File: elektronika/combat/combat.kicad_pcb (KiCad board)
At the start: 2 copper layers, 8 parts, among them J1 Conn_01x04_Pin, U2 TB6612FNG, U3 AMS1117, U3 L78M05CDT, U4 przetwornica

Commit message: płytka pcb bez footprinta
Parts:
- removed U2: TB6612FNG, Package_SO:SSOP-24_5.3x8.2mm_P0.65mm
- removed the U3 at (195.0, 100.7)
- removed the U3 at (163.5, 115.4)
- added J2: naped_prawy, TerminalBlock:TerminalBlock_MaiXu_MX126-5.0-02P_1x02_P5.00mm, F.Cu at (196.5, 137.0)
- added J3: naped_lewy, TerminalBlock:TerminalBlock_MaiXu_MX126-5.0-02P_1x02_P5.00mm, F.Cu at (196.5, 147.1)
- added TB1: POLOLU-713, foots:SHIELD_POLOLU-713, F.Cu at (241.7, 109.4)
- added U1: ESP32-S3-WROOM-1, Espressif:ESP32-S3-WROOM-1, F.Cu at (222.4, 115.1)
- added U3: AMS1117, Package_TO_SOT_SMD:SOT-223-3_TabPin2, F.Cu at (197.4, 156.4)
- R1: value 1k -> 240
- R2: value 1k -> 390
- moved U4 66.3 mm to (208.2, 149.2)
- moved R2 53.7 mm to (207.1, 160.2)
- moved R1 53.7 mm to (207.1, 157.7)
- moved D1 45.2 mm to (210.9, 158.5)
- moved J1 40.5 mm to (207.3, 134.3)
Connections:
- J1 pad 1: unconnected-(J1-Pin_1-Pad1) -> RX
- J1 pad 2: unconnected-(J1-Pin_2-Pad2) -> TX
- J1 pad 3: unconnected-(J1-Pin_3-Pad3) -> +5V
- J1 pad 4: unconnected-(J1-Pin_4-Pad4) -> GND

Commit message: gotowy footprint
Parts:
- added C1: 10uF, Capacitor_SMD:C_0805_2012Metric_Pad1.18x1.45mm_HandSolder, F.Cu at (205.5, 137.3)
- added C2: 22uF, Capacitor_SMD:C_1210_3225Metric_Pad1.33x2.70mm_HandSolder, F.Cu at (206.1, 133.6)
- added C5: 1u, Capacitor_SMD:C_0603_1608Metric, F.Cu at (159.5, 104.5)
- added D2: RED, LED_SMD:LED_0603_1608Metric, F.Cu at (201.1, 132.8)
- added D3: GREEN, LED_SMD:LED_0603_1608Metric, F.Cu at (201.1, 135.4)
- added D4: BLUE, LED_SMD:LED_0603_1608Metric, F.Cu at (201.1, 138.0)
- added H1: MountingHole, MountingHole:MountingHole_3.2mm_M3, F.Cu at (102.0, 103.5)
- added H2: MountingHole, MountingHole:MountingHole_3.2mm_M3, F.Cu at (103.0, 91.0)
- added H3: MountingHole, MountingHole:MountingHole_3.2mm_M3, F.Cu at (100.5, 122.0)
- added H4: MountingHole, MountingHole:MountingHole_3.2mm_M3, F.Cu at (101.0, 112.5)
- added J4: USB_C_Receptacle_USB2.0_14P, Connector_USB:USB_C_Receptacle_HRO_TYPE-C-31-M-12, F.Cu at (159.9, 123.9)
- added J5: Screw_Terminal_01x03, PCM_SparkFun-Connector:ScrewTerminal_1x03_P3.5mm_Blue, F.Cu at (136.0, 128.0)
- added J6: programator caveman, Connector_PinHeader_2.54mm:PinHeader_2x04_P2.54mm_Vertical, F.Cu at (215.0, 133.4)
- added J7: zasilanie, PCM_SparkFun-Connector:ScrewTerminal_1x02_P3.5mm_Blue, F.Cu at (212.9, 99.6)
- added R10: 5.1K, Resistor_SMD:R_0603_1608Metric, F.Cu at (152.0, 136.9)
- added R11: 5.1K, Resistor_SMD:R_0603_1608Metric, F.Cu at (152.0, 139.4)
- added R5: 5.1K, Resistor_SMD:R_0603_1608Metric, F.Cu at (152.0, 126.9)
- added R6: 1k, Resistor_SMD:R_0603_1608Metric, F.Cu at (152.0, 129.4)
- added R7: 1k, Resistor_SMD:R_0603_1608Metric, F.Cu at (152.0, 131.9)
- added R8: 5.1K, Resistor_SMD:R_0603_1608Metric, F.Cu at (152.0, 134.4)
- added SW1: SW_DIP_x01, foots:gownoklik, F.Cu at (155.4, 69.4)
- added SW3: SW_DIP_x01, foots:gownoklik, F.Cu at (189.5, 70.5)
- added U2: kontroler_bldc, foots:BLDC, F.Cu at (134.6, 74.5)
- J1: value Conn_01x04_Pin -> odbiornik
- J2, J3: footprint TerminalBlock:TerminalBlock_MaiXu_MX126-5.0-02P_1x02_P5.00mm -> PCM_SparkFun-Connector:ScrewTerminal_1x02_P3.5mm_Blue
- R1: value 240 -> 390
- R2: value 390 -> 240
- U3: value AMS1117 -> stabilizator
- moved U4 67.8 mm to (204.5, 81.5)
- moved R1 65.7 mm to (152.0, 121.9)
- moved R2 65.7 mm to (152.0, 124.4)
- moved U1 61.7 mm to (172.5, 78.8)
- moved TB1 61.7 mm to (180.3, 115.9)
- moved D1 51.5 mm to (161.4, 144.5)
- moved J3 48.6 mm to (201.9, 98.9)
- moved J2 38.3 mm to (192.7, 98.9)
- moved U3 25.8 mm to (182.0, 135.8)
- moved J1 17.0 mm to (191.5, 140.4)
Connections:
- J2 pad 1: unconnected-(J2-Pin_1-Pad1) -> B01
- J2 pad 2: unconnected-(J2-Pin_2-Pad2) -> B02
- J3 pad 1: unconnected-(J3-Pin_1-Pad1) -> A01
- J3 pad 2: unconnected-(J3-Pin_2-Pad2) -> A02
- TB1 pad 10: unconnected-(TB1-PWMB-Pad10) -> GPIO10
- TB1 pad 11: unconnected-(TB1-BIN2-Pad11) -> GPIO9
- TB1 pad 12: unconnected-(TB1-BIN1-Pad12) -> GPIO8
- TB1 pad 13: unconnected-(TB1-~{STBY}-Pad13) -> 3V3
- TB1 pad 14: unconnected-(TB1-AIN1-Pad14) -> GPIO5
- TB1 pad 15: unconnected-(TB1-AIN2-Pad15) -> GPIO6
- TB1 pad 16: unconnected-(TB1-PWMA-Pad16) -> GPIO7
- TB1 pad 2: unconnected-(TB1-VCC-Pad2) -> 3V3
- TB1 pad 3: unconnected-(TB1-AO1-Pad3) -> A01
- TB1 pad 4: unconnected-(TB1-AO2-Pad4) -> A02
- TB1 pad 5: unconnected-(TB1-BO2-Pad5) -> B02
- TB1 pad 6: unconnected-(TB1-BO1-Pad6) -> B01
- TB1 pad 7: unconnected-(TB1-VMOT-Pad7) -> 11.1V
- U1 pad 1: Net-(U1-GND-Pad1) -> GND
- U1 pad 10: unconnected-(U1-GPIO17/U1TXD/ADC2_CH6-Pad10) -> RX
- U1 pad 11: unconnected-(U1-GPIO18/U1RXD/ADC2_CH7/CLK_OUT3-Pad11) -> TX
- U1 pad 12: unconnected-(U1-GPIO8/TOUCH8/ADC1_CH7/SUBSPICS1-Pad12) -> GPIO8
- U1 pad 13: unconnected-(U1-GPIO19/U1RTS/ADC2_CH8/CLK_OUT2/USB_D--Pad13) -> D-
- U1 pad 14: unconnected-(U1-GPIO20/U1CTS/ADC2_CH9/CLK_OUT1/USB_D+-Pad14) -> D+
- U1 pad 17: unconnected-(U1-GPIO9/TOUCH9/ADC1_CH8/FSPIHD/SUBSPIHD-Pad17) -> GPIO9
- U1 pad 18: unconnected-(U1-GPIO10/TOUCH10/ADC1_CH9/FSPICS0/FSPIIO4/SUBSPICS0-Pad18) -> GPIO10
- U1 pad 2: unconnected-(U1-3V3-Pad2) -> +3.3V
- U1 pad 23: unconnected-(U1-GPIO21-Pad23) -> GPIO21
- U1 pad 27: unconnected-(U1-GPIO0/BOOT-Pad27) -> GPIO0
- U1 pad 3: unconnected-(U1-EN-Pad3) -> EN
- U1 pad 4: unconnected-(U1-GPIO4/TOUCH4/ADC1_CH3-Pad4) -> ePWM
- U1 pad 40: Net-(U1-GND-Pad1) -> GND
- U1 pad 41: Net-(U1-GND-Pad1) -> GND
- U1 pad 5: unconnected-(U1-GPIO5/TOUCH5/ADC1_CH4-Pad5) -> GPIO5
- U1 pad 6: unconnected-(U1-GPIO6/TOUCH6/ADC1_CH5-Pad6) -> GPIO6
- U1 pad 7: unconnected-(U1-GPIO7/TOUCH7/ADC1_CH6-Pad7) -> GPIO7
- U4 pad 1: (no net) -> GND

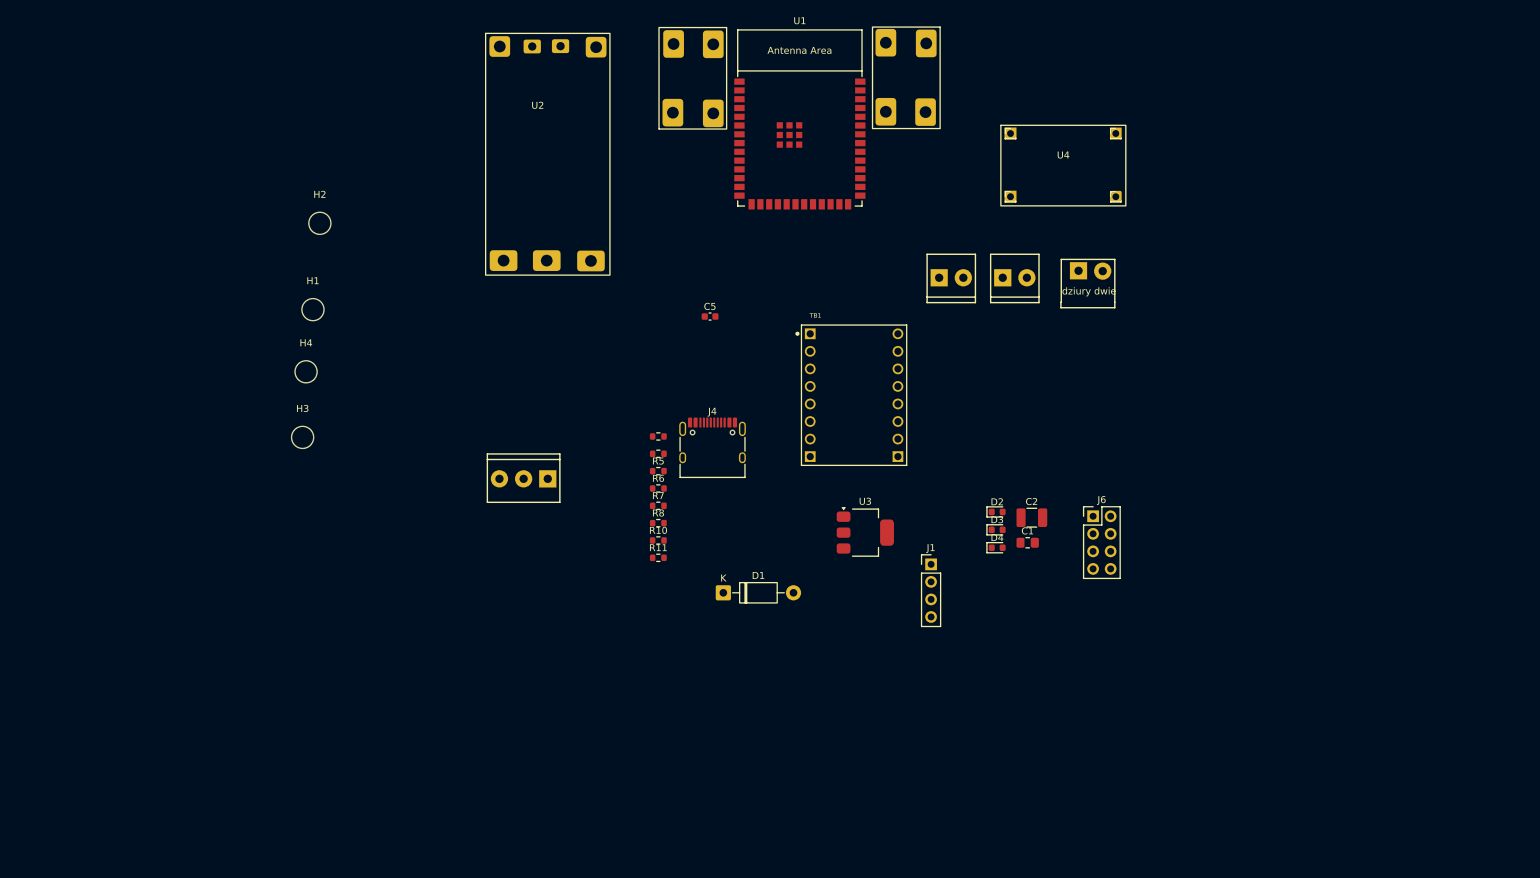
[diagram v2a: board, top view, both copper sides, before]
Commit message: lepsza wersja pcb, layout jeszcze do zrobienia
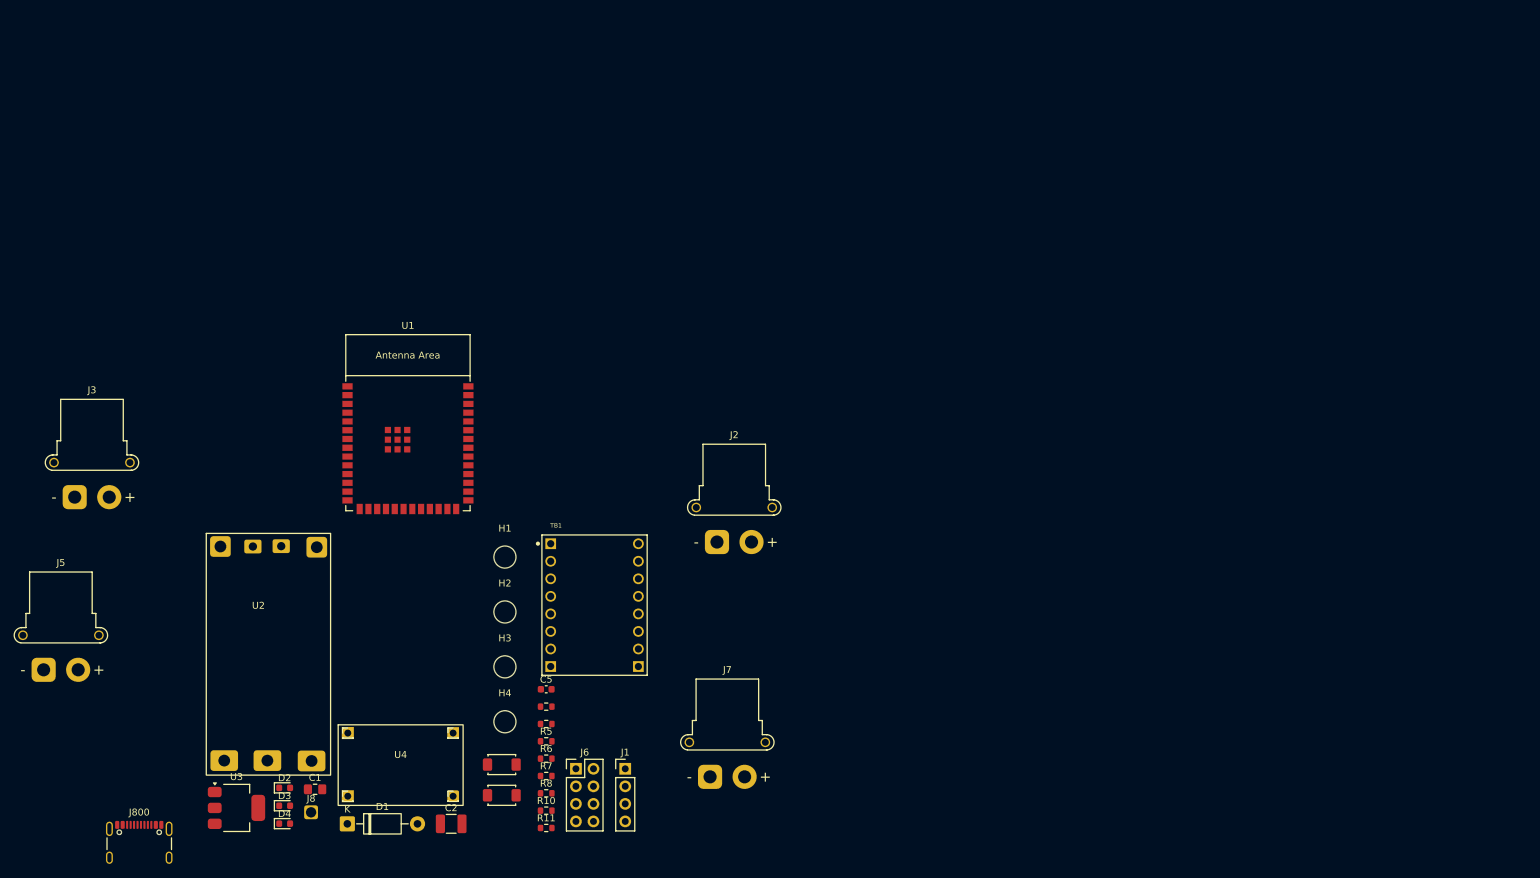
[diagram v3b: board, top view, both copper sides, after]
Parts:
- removed J4: USB_C_Receptacle_USB2.0_14P, Connector_USB:USB_C_Receptacle_HRO_TYPE-C-31-M-12
- removed SW1, SW3: SW_DIP_x01, foots:gownoklik
- added J8: Conn_01x01_Pin, Connector_Wire:SolderWire-0.1sqmm_1x01_D0.4mm_OD1mm, F.Cu at (101.7, 176.3)
- added J800: USB_C_Receptacle_USB2.0_16P, Connector_USB:USB_C_Receptacle_GCT_USB4105-xx-A_16P_TopMnt_Horizontal, F.Cu at (76.8, 181.8)
- added S1: Tactile Button, 160gf, PCM_JLCPCB:SW_TS-1088-AR02016, F.Cu at (129.3, 169.4)
- added S2: Tactile Button, 160gf, PCM_JLCPCB:SW_TS-1088-AR02016, F.Cu at (129.3, 173.8)
- J1: value odbiornik -> odbiornik
- J2, J3: footprint PCM_SparkFun-Connector:ScrewTerminal_1x02_P3.5mm_Blue -> Connector_AMASS:AMASS_XT30PW-F_1x02_P2.50mm_Horizontal
- J5: value Screw_Terminal_01x03 -> wyjscie do silnika +-; footprint PCM_SparkFun-Connector:ScrewTerminal_1x03_P3.5mm_Blue -> Connector_AMASS:AMASS_XT30PW-F_1x02_P2.50mm_Horizontal
- J6: value programator caveman -> Conn_02x04_Odd_Even
- J7: value zasilanie -> zasilanie xt30; footprint PCM_SparkFun-Connector:ScrewTerminal_1x02_P3.5mm_Blue -> Connector_AMASS:AMASS_XT30PW-F_1x02_P2.50mm_Horizontal
- U3: value stabilizator -> AMS1117
- moved J3 138.1 mm to (67.5, 130.7)
- moved U4 129.4 mm to (108.5, 168.3)
- moved D2 110.6 mm to (97.9, 172.7)
- moved D3 110.6 mm to (97.9, 175.3)
- moved D4 110.6 mm to (97.9, 177.9)
- moved C1 109.2 mm to (102.3, 173.0)
- moved U3 99.4 mm to (90.9, 175.7)
- moved C2 95.0 mm to (122.0, 178.0)
- moved J7 89.2 mm to (159.5, 171.2)
- moved J6 83.3 mm to (140.1, 170.0)
- moved U2 82.9 mm to (94.1, 146.8)
- moved J5 78.1 mm to (63.0, 155.7), turned to 0 degrees
- moved U1 71.9 mm to (115.8, 122.9)
- moved D1 63.9 mm to (107.0, 178.0)
- moved H2 62.3 mm to (129.8, 147.3)
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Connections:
- J7 pad 1: unconnected-(J7-Pin_1-Pad1) -> GND
- J7 pad 2: unconnected-(J7-Pin_2-Pad2) -> 11.1V
- U1 pad 13: D- -> USB.D-
- U1 pad 14: D+ -> USB.D+
- U2 pad 5: Net-(J5-Pin_3) -> Net-(J5-Pin_2)
- U2 pad 6: Net-(J5-Pin_2) -> Net-(J8-Pin_1)

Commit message: pcb v1.0
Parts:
- added J4: buzzer, Connector_PinSocket_2.54mm:PinSocket_1x02_P2.54mm_Vertical, F.Cu at (128.5, 124.5)
- D2: value RED -> led
- D3: value GREEN -> led
- D4: value BLUE -> led
- J2, J3, J5, J7: footprint Connector_AMASS:AMASS_XT30PW-F_1x02_P2.50mm_Horizontal -> Connector_AMASS:AMASS_XT30U-F_1x02_P5.0mm_Vertical
- J6: value Conn_02x04_Odd_Even -> programator
- J8: value Conn_01x01_Pin -> pwm silnika broni; footprint Connector_Wire:SolderWire-0.1sqmm_1x01_D0.4mm_OD1mm -> Connector_PinHeader_2.54mm:PinHeader_1x01_P2.54mm_Vertical
- J800: value USB_C_Receptacle_USB2.0_16P -> usb c
- S1, S2: value Tactile Button, 160gf -> przycisk
- TB1: value POLOLU-713 -> mostek h
- U3: value AMS1117 -> satbilizator
- moved J7 87.4 mm to (76.0, 145.5), turned to 90 degrees
- moved R8 76.7 mm to (102.3, 104.5)
- moved H3 75.0 mm to (76.0, 103.0)
- moved U3 74.7 mm to (139.0, 118.5), turned to -90 degrees
- moved C2 72.9 mm to (138.0, 106.8)
- moved C1 72.7 mm to (132.5, 106.8)
- moved J1 70.9 mm to (128.7, 101.5), turned to 90 degrees
- moved S2 69.2 mm to (102.5, 110.1), turned to -90 degrees
- moved D1 68.3 mm to (145.5, 121.6), turned to 90 degrees
- moved C5 66.6 mm to (102.2, 101.0), turned to 180 degrees
- moved R10 64.5 mm to (84.0, 137.5)
- moved R11 63.2 mm to (84.2, 142.0)
- moved J8 59.7 mm to (77.0, 122.0)
- moved R5 57.5 mm to (128.3, 109.0)
- moved S1 56.2 mm to (102.5, 120.0), turned to 90 degrees
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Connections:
- U1 pad 32: unconnected-(U1-MTCK/GPIO39/CLK_OUT3/SUBSPICS1-Pad32) -> john

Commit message: PCB v1.2
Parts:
- moved U4 34.0 mm to (109.3, 132.9), turned to 0 degrees
- moved TB1 26.1 mm to (141.5, 132.5)
- moved J800 19.6 mm to (90.0, 144.5), turned to 0 degrees
- moved H1 18.0 mm to (148.5, 145.5)
- moved H4 14.5 mm to (78.0, 144.0)
- moved J7 10.5 mm to (75.5, 135.0)
- moved R2 7.84 mm to (136.0, 119.1), turned to 90 degrees
- moved R11 7.07 mm to (89.2, 137.0)
- moved J6 7.07 mm to (129.7, 146.8)
- moved R1 6.89 mm to (136.0, 115.4), turned to 90 degrees
- moved C1 6.51 mm to (138.0, 110.2)
- moved C2 6.51 mm to (143.6, 110.2)
- moved D1 2.64 mm to (148.0, 120.7)
- moved U3 2.55 mm to (141.5, 118.0)
- moved D4 0.50 mm to (101.8, 137.5), turned to 0 degrees
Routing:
- net (no net): track 0.00 -> 59.4 mm
- added copper zone on B.Cu, net GND
- added copper zone on F.Cu, net GND
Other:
- board outline added: 80 x 50 mm

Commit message: pierwsze scieżki
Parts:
- D2: value led -> RED
- D3: value led -> GREEN
- D4: value led -> BLUE
- J6: value programator -> Conn_02x04_Odd_Even
- J8: value pwm silnika broni -> Conn_01x01_Pin
- J800: value usb c -> USB_C_Receptacle_USB2.0_16P
- S1, S2: value przycisk -> Tactile Button, 160gf
- TB1: value mostek h -> POLOLU-713
- U3: value satbilizator -> AMS1117
- moved D3 39.9 mm to (133.2, 107.1), turned to 180 degrees
- moved R5 33.2 mm to (106.2, 133.8), turned to 180 degrees
- moved D4 22.7 mm to (122.3, 127.7), turned to 180 degrees
- moved R7 15.0 mm to (118.5, 127.7)
- moved U4 12.8 mm to (121.6, 136.4), turned to 180 degrees
- moved C5 12.6 mm to (103.2, 113.5), turned to 0 degrees
- moved C1 12.4 mm to (141.4, 122.2)
- moved S2 6.43 mm to (102.5, 103.7)
- moved R6 6.38 mm to (129.1, 107.2)
- moved D2 6.20 mm to (102.2, 133.7)
- moved C2 5.84 mm to (139.1, 106.5)
- moved R8 5.29 mm to (104.2, 109.4), turned to -90 degrees
- moved R2 5.17 mm to (131.5, 116.5), turned to 180 degrees
- moved R1 4.60 mm to (131.5, 114.5), turned to 0 degrees
- moved TB1 4.40 mm to (137.1, 132.8)
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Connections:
- J2 pad 1: B01 -> B02
- J2 pad 2: B02 -> B01
- R6 pad 1: +3V3 -> +3.3V
- R8 pad 1: +3V3 -> +3.3V
- U2 pad 5: Net-(J5-Pin_2) -> Net-(J8-Pin_1)
- U2 pad 6: Net-(J8-Pin_1) -> Net-(J5-Pin_2)
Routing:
- net +5V: track 0.00 -> 83.7 mm, vias 0 -> 4
- net +3.3V: track 0.00 -> 75.4 mm, vias 0 -> 5
- net 11.1V: track 0.00 -> 50.1 mm, vias 0 -> 4
- net A01: track 0.00 -> 39.4 mm, vias 0 -> 1
- net USB.D+: track 0.00 -> 38.5 mm, vias 0 -> 2
- net TX: track 0.00 -> 36.5 mm, vias 0 -> 2
- net USB.D-: track 0.00 -> 36.4 mm, vias 0 -> 2
- net RX: track 0.00 -> 34.6 mm, vias 0 -> 3
- net A02: track 0.00 -> 34.2 mm
- net Net-(J8-Pin_1): track 0.00 -> 30.5 mm, vias 0 -> 1
- net ePWM: track 0.00 -> 29.4 mm, vias 0 -> 3
- net GPIO7: track 0.00 -> 27.4 mm, vias 0 -> 2
- net GPIO0: track 0.00 -> 25.0 mm, vias 0 -> 2
- net B02: track 0.00 -> 24.0 mm
- net B01: track 0.00 -> 21.5 mm
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- added copper zone on F.Cu, net 11.1V
- added copper zone on B.Cu, net Net-(J5-Pin_1)
- added copper zone on F.Cu, net Net-(J5-Pin_2)
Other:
- board size 80 x 50 mm -> 76 x 50 mm

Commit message: PCB 1.0 complete
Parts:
- moved J6 53.6 mm to (98.0, 103.8)
- moved D3 40.7 mm to (138.9, 147.3), turned to 0 degrees
- moved R6 39.5 mm to (138.9, 145.4)
- moved J1 32.1 mm to (105.5, 123.7), turned to -90 degrees
- moved S2 27.7 mm to (98.0, 130.9), turned to 90 degrees
- moved J8 25.7 mm to (94.2, 102.3)
- moved D2 24.4 mm to (125.7, 127.0), turned to 180 degrees
- moved C2 24.1 mm to (141.2, 130.5)
- moved U3 22.3 mm to (139.2, 137.8), turned to 0 degrees
- moved C1 22.1 mm to (136.1, 143.6), turned to -90 degrees
- moved D1 20.8 mm to (145.7, 139.4)
- moved R1 20.5 mm to (140.2, 133.1), turned to 180 degrees
- moved J4 19.5 mm to (135.2, 102.3)
- moved R2 17.4 mm to (136.8, 133.1)
- moved R5 16.9 mm to (121.7, 126.9), turned to 0 degrees
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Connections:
- J2 pad 1: B02 -> A02
- J2 pad 2: B01 -> A01
- J3 pad 1: A01 -> B01
- J3 pad 2: A02 -> B02
- J6 pad 1: 3V3 -> +3.3V
- TB1 pad 10: GPIO10 -> GPIO2
- TB1 pad 11: GPIO9 -> GPIO1
- TB1 pad 12: GPIO8 -> GPIO41
- TB1 pad 13: 3V3 -> +3.3V
- TB1 pad 14: GPIO5 -> GPIO40
- TB1 pad 15: GPIO6 -> GPIO39
- TB1 pad 16: GPIO7 -> GPIO38
- TB1 pad 2: 3V3 -> +3.3V
- U1 pad 12: GPIO8 -> unconnected-(U1-GPIO8/TOUCH8/ADC1_CH7/SUBSPICS1-Pad12)
- U1 pad 17: GPIO9 -> unconnected-(U1-GPIO9/TOUCH9/ADC1_CH8/FSPIHD/SUBSPIHD-Pad17)
- U1 pad 18: GPIO10 -> unconnected-(U1-GPIO10/TOUCH10/ADC1_CH9/FSPICS0/FSPIIO4/SUBSPICS0-Pad18)
- U1 pad 31: unconnected-(U1-GPIO38/FSPIWP/SUBSPIWP-Pad31) -> GPIO38
- U1 pad 32: john -> GPIO39
- U1 pad 33: unconnected-(U1-MTDO/GPIO40/CLK_OUT2-Pad33) -> GPIO40
- U1 pad 34: unconnected-(U1-MTDI/GPIO41/CLK_OUT1-Pad34) -> GPIO41
- U1 pad 35: unconnected-(U1-MTMS/GPIO42-Pad35) -> GPIO1
- U1 pad 38: unconnected-(U1-GPIO2/TOUCH2/ADC1_CH1-Pad38) -> GPIO2
- U1 pad 39: unconnected-(U1-GPIO1/TOUCH1/ADC1_CH0-Pad39) -> john
- U1 pad 5: GPIO5 -> unconnected-(U1-GPIO5/TOUCH5/ADC1_CH4-Pad5)
- U1 pad 6: GPIO6 -> unconnected-(U1-GPIO6/TOUCH6/ADC1_CH5-Pad6)
- U1 pad 7: GPIO7 -> unconnected-(U1-GPIO7/TOUCH7/ADC1_CH6-Pad7)
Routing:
- net +3.3V: track 75.4 -> 136.1 mm, vias 5 -> 9
- net B01: track 21.5 -> 50.3 mm
- net GPIO7: track 27.4 -> 0.00 mm, vias 2 -> 0
- net 11.1V: track 50.1 -> 75.2 mm, vias 4 -> 2
- net Net-(J8-Pin_1): track 30.5 -> 7.46 mm, vias 1 -> 0
- net ePWM: track 29.4 -> 49.2 mm, vias 3 -> 1
- net B02: track 24.0 -> 43.5 mm
- net EN: track 15.6 -> 32.5 mm, vias 1 -> 4
- net (no net): track 59.4 -> 45.5 mm, vias 0 -> 1
- net USB.D+: track 38.5 -> 27.2 mm
- net TX: track 36.5 -> 27.5 mm, vias 2 -> 1
- net GPIO38: track 0.00 -> 8.93 mm, vias 0 -> 2
- net GPIO0: track 25.0 -> 33.9 mm
- net GPIO39: track 0.00 -> 7.67 mm, vias 0 -> 2
- net A01: track 39.4 -> 32.2 mm, vias 1 -> 0
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- added copper zone on F.Cu, net Net-(J5-Pin_1)
- added copper zone on B.Cu, net Net-(J5-Pin_2)
- removed copper zone on B.Cu, net Net-(J5-Pin_1)
- removed copper zone on F.Cu, net Net-(J5-Pin_2)

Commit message: wersja nadajaca sie do sprawdzania
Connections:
- J4 pad 1: john -> GPIO1
- U1 pad 39: john -> GPIO1
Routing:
- net john: track 8.92 -> 0.00 mm
- net GPIO1: track 4.24 -> 13.2 mm
- net RX: track 40.8 -> 40.0 mm
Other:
- board text added: "+"
- board text added: "-"
